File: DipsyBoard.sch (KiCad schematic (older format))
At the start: 31 parts, among them CON1 SD_Card, P1 USB_OTG, P2 CONN_01X16, P3 CONN_01X16, SW1 SW_PUSH, U1 STM32L486Rx-LQFP64, U2 LD1117S50TR, U4 PUSBMxX4, U5 TPS56x200, Y1 16MHz

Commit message: Last changes
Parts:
- removed C10, C11: 22pF, Capacitors_SMD:C_0603, symbol C_Small
- removed C15: 0.1u, Capacitors_SMD:C_0603, symbol C_Small
- removed C16: 22uF, Capacitors_SMD:C_1206, symbol C
- removed L1: 3.3uH, SMD_Packages:SMD-1210_Pol, symbol L_Small
- removed P2, P3: CONN_01X16, Pin_Headers:Pin_Header_Straight_1x16, symbol CONN_01X16
- removed R1: 33.2k, Resistors_SMD:R_0603, symbol R
- removed R2: 10.0k, Resistors_SMD:R_0603, symbol R
- removed SW1: SW_PUSH, Buttons_Switches_ThroughHole:SW_PUSH, symbol SW_PUSH
- removed U5: TPS56x200, Housings_SOT-23_SOT-143_TSOT-6:SOT-23-6, symbol TPS56x200
- removed Y1: 16MHz, Crystals:Crystal_SMD_0603_4Pads, symbol Crystal_Small
- added C18: 0.1uF, w_smd_cap:c_0603, symbol C
- added P2, P3: CONN_01X19, w_pin_strip:pin_strip_19, symbol CONN_01X19
- added P6: JTAG, engstad:conn-jtag-0.05, symbol CONN_02X05
- added SW1: RESET, Buttons_Switches_SMD:SW_SPST_EVPBF, symbol Switch_DPST
- added U3: NCP1117DT33G, w_smd_trans:sot223, symbol LD1117S50TR
- added X1: XTAL, engstad:cstce-v-c, symbol CRYSTAL_SMD
- C1, C5, C6, C7, C8, C9: footprint Capacitors_SMD:C_0603 -> w_smd_cap:c_0603
- C12, C13, C14, C2, C3, C4: footprint Capacitors_SMD:C_0805 -> w_smd_cap:c_0805
- C17: footprint Capacitors_SMD:C_1206 -> w_smd_cap:c_1206
- CON1: footprint Connect:SD_Card_Receptacle -> xess:xess-SCHD3A0100
- P1: footprint Connect:USB_B -> w_conn_pc:conn_usb_B_mini_smd
- U2: value LD1117S50TR -> NCP1117ST50T3G; footprint Housings_SOT-23_SOT-143_TSOT-6:SOT-23 -> w_smd_trans:sot223
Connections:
- net labels added: +5V, OTG_FS_D+, OTG_FS_D-, PVD
- net labels removed: D4/PVD, OTG_FS_DM, OTG_FS_DP, OTG_FS_SOF, OTG_FS_VBUS, SENSE, SW
- wire segments 65 -> 57
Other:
- moved on the sheet: C14, C17

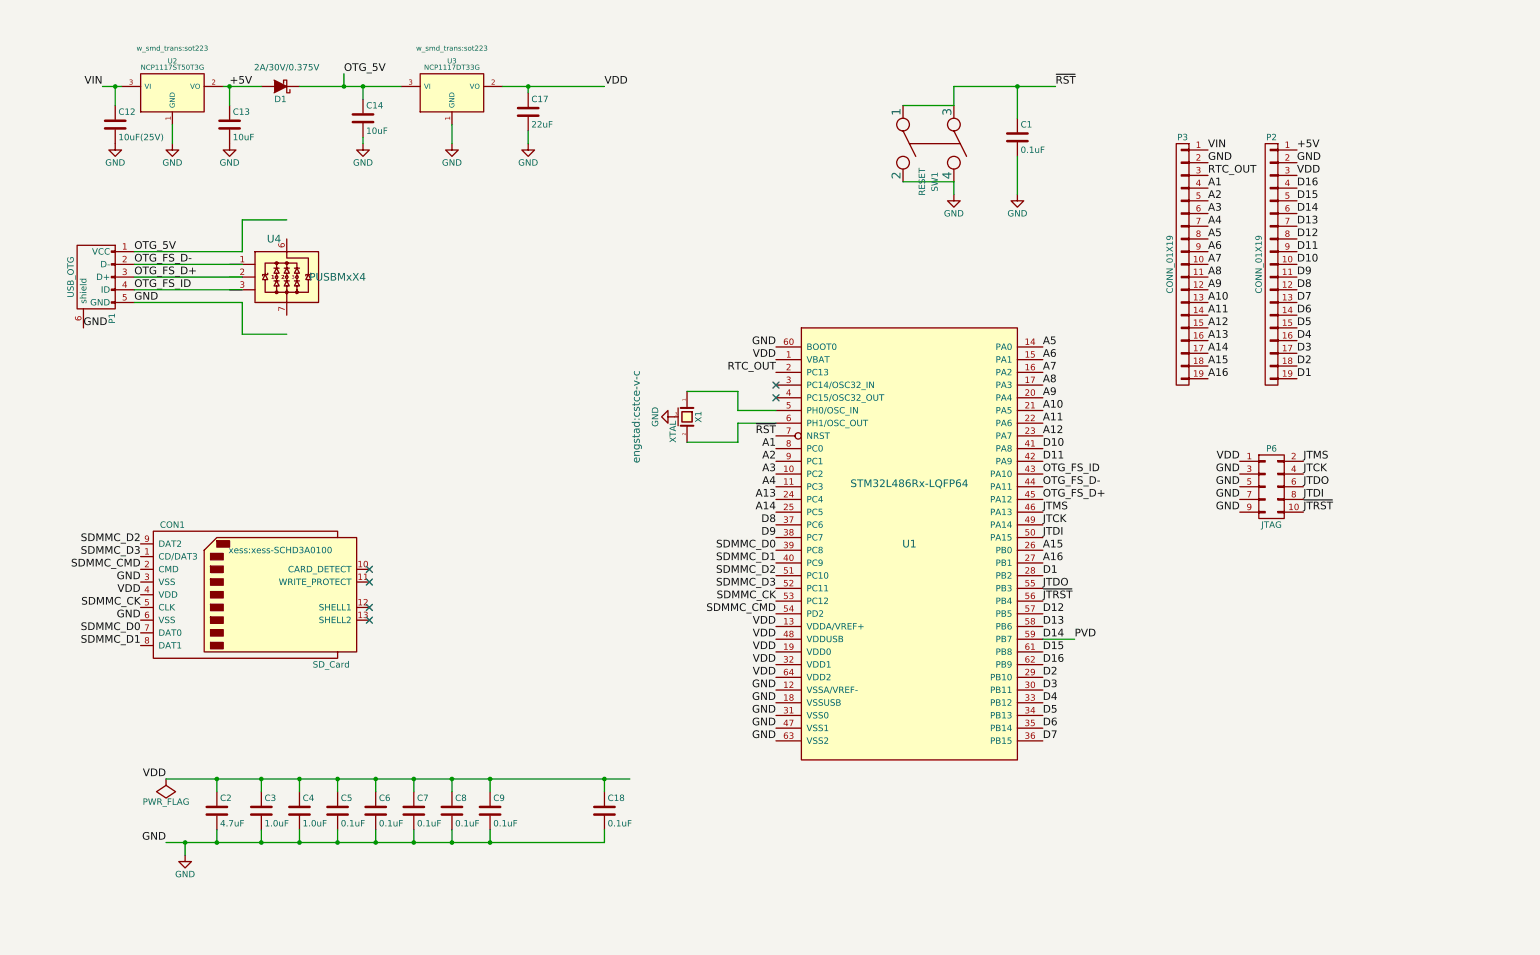
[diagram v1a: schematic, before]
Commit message: Changes of power source
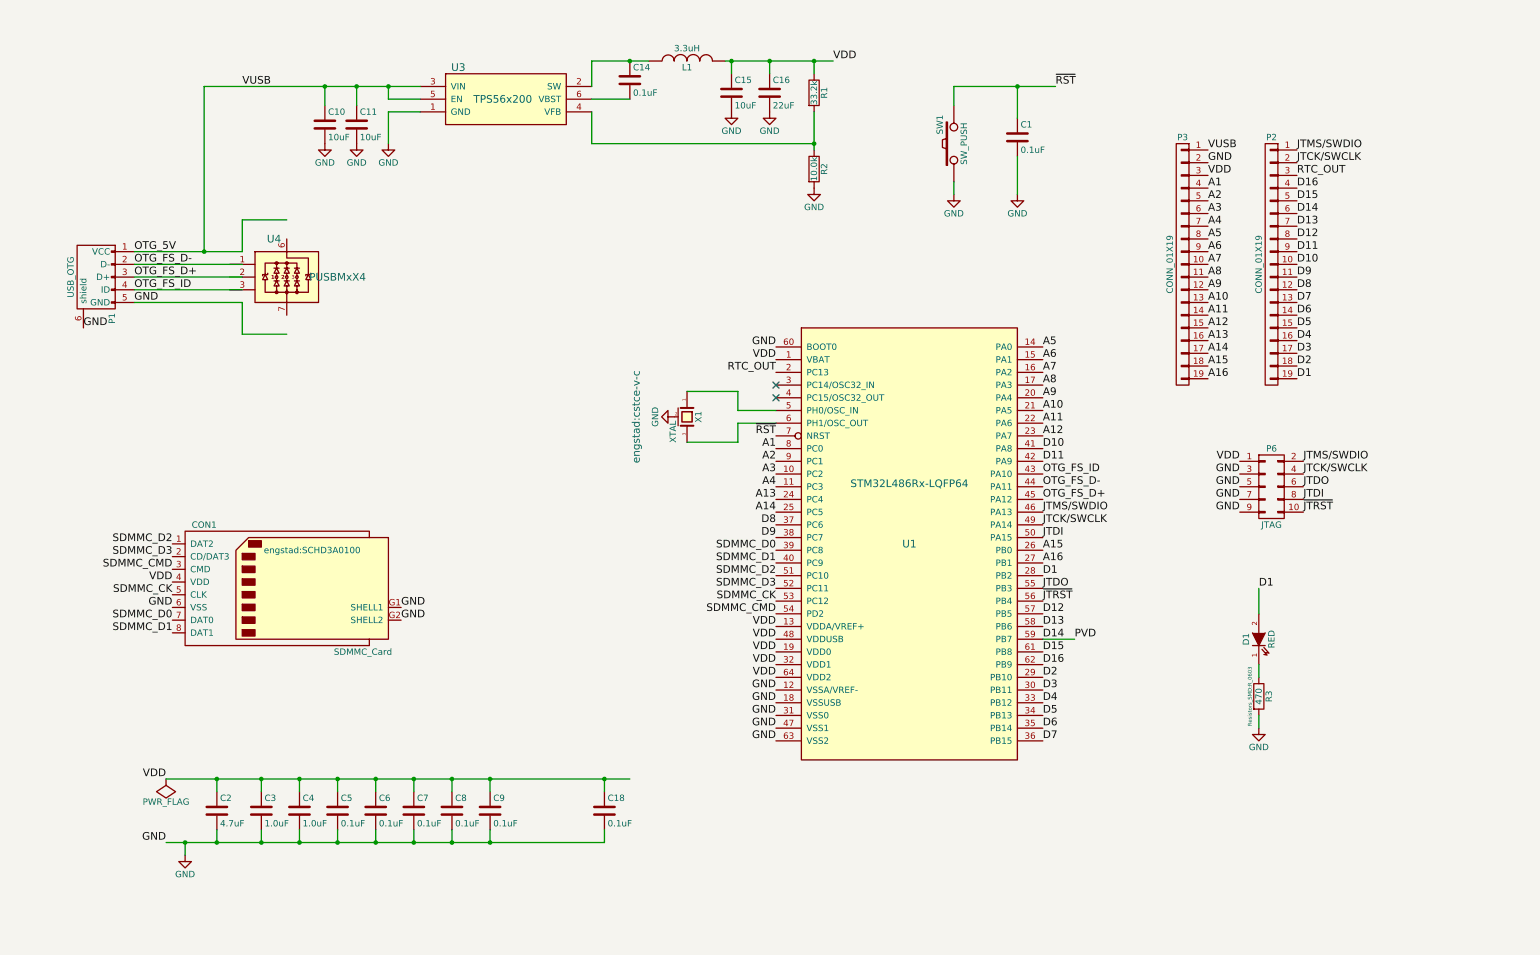
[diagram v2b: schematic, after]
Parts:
- removed C12: 10uF(25V), w_smd_cap:c_0805, symbol C
- removed C13: 10uF, w_smd_cap:c_0805, symbol C
- removed C17: 22uF, w_smd_cap:c_1206, symbol C
- removed CON1: SD_Card, xess:xess-SCHD3A0100, symbol SD_Card
- removed D1: 2A/30V/0.375V, Diodes_SMD:SOD-123, symbol D_Schottky
- removed SW1: RESET, Buttons_Switches_SMD:SW_SPST_EVPBF, symbol Switch_DPST
- removed U2: NCP1117ST50T3G, w_smd_trans:sot223, symbol LD1117S50TR
- removed U3: NCP1117DT33G, w_smd_trans:sot223, symbol LD1117S50TR
- removed X1: XTAL, engstad:cstce-v-c, symbol CRYSTAL_SMD
- added C10, C11, C15: 10uF, Capacitors_SMD:C_0805, symbol C
- added C16: 22uF, Capacitors_SMD:C_1206, symbol C
- added CON1: SDMMC_Card, engstad:SCHD3A0100, symbol SDMMC_Card
- added D1: RED, LEDs:LED-0805, symbol LED
- added L1: 3.3uH, engstad:inductor-smd-1212, symbol INDUCTOR
- added R1: 33.2k, Resistors_SMD:R_0603, symbol R
- added R2: 10.0k, Resistors_SMD:R_0603, symbol R
- added R3: 470, Resistors_SMD:R_0603, symbol R
- added SW1: SW_PUSH, engstad:tactile-switch-te-147873-2, symbol SW_PUSH
- added U3: TPS56x200, Housings_SOT-23_SOT-143_TSOT-6:SOT-23-6, symbol TPS56x200
- added X1: XTAL, engstad:cstce-v-c, symbol crystal-resonator-smd
- C1, C18, C5, C6, C7, C8, C9: footprint w_smd_cap:c_0603 -> Capacitors_SMD:C_0603
- C14: value 10uF -> 0.1uF; footprint w_smd_cap:c_0805 -> Capacitors_SMD:C_0603
- C2, C3, C4: footprint w_smd_cap:c_0805 -> Capacitors_SMD:C_0805
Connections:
- net labels added: JTCK/SWCLK, JTMS/SWDIO, VUSB
- net labels removed: +5V, JTCK, JTMS, VIN
- wire segments 57 -> 63
- no-connect marks 6 -> 2

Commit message: latest - including v0.1
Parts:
- added C? (x2): 22uF, Capacitors_SMD:C_0805, symbol C
- added L?: 470nF, symbol L_Small
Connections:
- wire segments 63 -> 75
- no-connect marks 2 -> 3
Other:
- moved on the sheet: CON1
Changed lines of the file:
@@
 Text Label 6450 4800 2    60   ~ 0
 SDMMC_D1
-Text Label 1700 5250 2    60   ~ 0
+Text Label 4650 5250 0    60   ~ 0
 SDMMC_D0
-Text Label 1700 5350 2    60   ~ 0
+Text Label 4650 5350 0    60   ~ 0
 SDMMC_D1
-Text Label 1700 4650 2    60   ~ 0
+Text Label 4650 4650 0    60   ~ 0
 SDMMC_D2
-Text Label 1700 4750 2    60   ~ 0
+Text Label 4650 4750 0    60   ~ 0
 SDMMC_D3
-Text Label 1700 4850 2    60   ~ 0
+Text Label 4650 4850 0    60   ~ 0
 SDMMC_CMD
-Text Label 1700 5050 2    60   ~ 0
+Text Label 4650 5050 0    60   ~ 0
 SDMMC_CK
 Text Label 6450 5200 2    60   ~ 0
@@
 Text Label 6450 4900 2    60   ~ 0
 SDMMC_D2
-Text Label 3500 5150 0    60   ~ 0
+Text Label 900  5150 2    60   ~ 0
 GND
-Text Label 1700 4950 2    60   ~ 0
+Text Label 4650 4950 0    60   ~ 0
 VDD
-Text Label 1700 5150 2    60   ~ 0
+Text Label 2700 5150 0    60   ~ 0
 GND
 Text Label 8550 3100 0    60   ~ 0
@@
 	2600 2100 2250 2100
 Wire Wire Line
-	2250 2100 2250 2350
-Wire Wire Line
-	2250 2350 1400 2350
+	2250 2350 2250 2100
+Wire Wire Line
+	1400 2350 2250 2350
 Text Label 1400 2350 0    60   ~ 0
 OTG_5V
@@
 Text Label 10100 4400 2    60   ~ 0
 GND
-Text Label 10100 4300 2    60   ~ 0
-GND
 Text Label 9850 1750 0    60   ~ 0
 VDD
 Text Label 9850 1650 0    60   ~ 0
 GND
-Text Label 10550 1750 0    60   ~ 0
-RTC_OUT
 $Comp
 L CONN_01X19 P2
@@
 	0    -1   -1   0
 $EndComp
-Text Label 3500 5250 0    60   ~ 0
+Text Label 900  5250 2    60   ~ 0
 GND
 $Comp
 L SDMMC_Card CON1
 U 1 1 560A8328
-P 2600 5050
-F 0 "CON1" H 1950 5600 50  0000 C CNN
-F 1 "SDMMC_Card" H 3200 4600 50  0000 C CNN
-F 2 "engstad:SCHD3A0100" H 2800 5400 50  0000 C CNN
-F 3 "" H 2600 5050 60  0000 C CNN
-	1    2600 5050
-	1    0    0    -1
+P 1800 5050
+F 0 "CON1" H 1150 5600 50  0000 C CNN
+F 1 "SDMMC_Card" H 2400 4600 50  0000 C CNN
+F 2 "engstad:SCHD3A0100" H 2000 5400 50  0000 C CNN
+F 3 "" H 1800 5050 60  0000 C CNN
+	1    1800 5050
+	-1   0    0    -1
 $EndComp
 $Comp
@@
 $EndComp
 Wire Wire Line
-	6750 1550 6750 1250
+	6750 1250 6750 1550
 Wire Wire Line
 	5000 1250 5000 1500
@@
 Text Label 10250 5000 0    60   ~ 0
 D1
+Wire Wire Line
+	2700 4950 4400 4950
+$Comp
+L C C?
+U 1 1 56166412
+P 4000 5600
+F 0 "C?" H 4025 5700 50  0000 L CNN
+F 1 "22uF" H 4025 5500 50  0000 L CNN
+F 2 "Capacitors_SMD:C_0805" H 4038 5450 30  0001 C CNN
+F 3 "" H 4000 5600 60  0000 C CNN
+	1    4000 5600
+	1    0    0    -1
+$EndComp
+$Comp
+L C C?
+U 1 1 56166609
+P 4250 5600
+F 0 "C?" H 4275 5700 50  0000 L CNN
+F 1 "22uF" H 4275 5500 50  0000 L CNN
+F 2 "Capacitors_SMD:C_0805" H 4288 5450 30  0001 C CNN
+F 3 "" H 4250 5600 60  0000 C CNN
+	1    4250 5600
+	1    0    0    -1
+$EndComp
+Wire Wire Line
+	4000 5450 4000 4950
+Connection ~ 4000 4950
+Wire Wire Line
+	4000 5750 4000 5800
+Wire Wire Line
+	4250 5750 4250 5800
+Wire Wire Line
+	4250 5450 4250 4950
+Connection ~ 4250 4950
+$Comp
+L GND #PWR?
+U 1 1 5616688A
+P 4000 5800
+F 0 "#PWR?" H 4000 5550 50  0001 C CNN
+F 1 "GND" H 4000 5650 50  0000 C CNN
+F 2 "" H 4000 5800 60  0000 C CNN
+F 3 "" H 4000 5800 60  0000 C CNN
+	1    4000 5800
+	1    0    0    -1
+$EndComp
+$Comp
+L GND #PWR?
+U 1 1 561668FC
+P 4250 5800
+F 0 "#PWR?" H 4250 5550 50  0001 C CNN
+F 1 "GND" H 4250 5650 50  0000 C CNN
+F 2 "" H 4250 5800 60  0000 C CNN
+F 3 "" H 4250 5800 60  0000 C CNN
+	1    4250 5800
+	1    0    0    -1
+$EndComp
+$Comp
+L L_Small L?
+U 1 1 561669CE
+P 4500 4950
+F 0 "L?" H 4530 4990 50  0000 L CNN
+F 1 "470nF" H 4530 4910 50  0000 L CNN
+F 2 "" H 4500 4950 60  0000 C CNN
+F 3 "" H 4500 4950 60  0000 C CNN
+	1    4500 4950
+	0    -1   -1   0
+$EndComp
+Wire Wire Line
+	4600 4950 4650 4950
+Wire Wire Line
+	2700 4650 4650 4650
+Wire Wire Line
+	2700 4750 4650 4750
+Wire Wire Line
+	2700 4850 4650 4850
+Wire Wire Line
+	2700 5050 4650 5050
+Wire Wire Line
+	2700 5250 4650 5250
+Wire Wire Line
+	2700 5350 4650 5350
+Text Label 10550 1750 0    60   ~ 0
+~JTRST
+NoConn ~ 10100 4300
 $EndSCHEMATC

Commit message: v0.2
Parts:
- removed C14: 0.1uF, Capacitors_SMD:C_0603, symbol C
- removed C15: 10uF, Capacitors_SMD:C_0805, symbol C
- removed C16: 22uF, Capacitors_SMD:C_1206, symbol C
- removed L1: 3.3uH, engstad:inductor-smd-1212, symbol INDUCTOR
- removed P2, P3: CONN_01X19, w_pin_strip:pin_strip_19, symbol CONN_01X19
- removed R1: 33.2k, Resistors_SMD:R_0603, symbol R
- removed R2: 10.0k, Resistors_SMD:R_0603, symbol R
- removed U3: TPS56x200, Housings_SOT-23_SOT-143_TSOT-6:SOT-23-6, symbol TPS56x200
- added C17, C19: 10pF, smd:SM0603, symbol C_Small
- added D2: DFLS240L, engstad:diode-smd-powerdi-123, symbol D_Schottky_Small
- added D3: GREEN, LEDs:LED-0805, symbol LED
- added JP1: JUMPER3, xess:xess-JP2, symbol JUMPER3
- added L3: Bead, smd:SM0805, symbol L_Small
- added P2: Analog, Pin_Headers:Pin_Header_Straight_1x16, symbol CONN_01X16
- added P3: Digital, Pin_Headers:Pin_Header_Straight_1x16, symbol CONN_01X16
- added P4: JLINK-SWD, xess:HDR_1x6, symbol CONN_01X06
- added P5: POWER, w_pin_strip:pin_socket_2, symbol CONN_01X02
- added R4: 10k, smd:SM0603, symbol R
- added R5: 470, smd:SM0603, symbol R
- added U2: NCP1117ST33T3G, TO_SOT_Packages_SMD:SOT-223, symbol NCP1117ST33T3G
- added U3: APX823, TO_SOT_Packages_SMD:SOT-23-5, symbol APX823
- added Y1: Crystal, armory:CRYSTAL-32k-B, symbol Crystal
- C1, C18, C5, C6, C7, C8, C9: footprint Capacitors_SMD:C_0603 -> smd:SM0603
- C10, C11, C2: footprint Capacitors_SMD:C_0805 -> smd:SM0805
- C12, C13: renamed from C?; footprint Capacitors_SMD:C_0805 -> smd:SM1206
- C3, C4: footprint Capacitors_SMD:C_0805 -> smd:SM0603
- L2: renamed from L?; value 470nF -> 470nH; footprint (none) -> smd:SM0603
- P1: footprint w_conn_pc:conn_usb_B_mini_smd -> engstad:usb-otg-short
- P6: value JTAG -> CORTEX-JTAG; footprint engstad:conn-jtag-0.05 -> engstad:smt-pin-header-02x05-127
- R3: footprint Resistors_SMD:R_0603 -> smd:SM0603
- U4: value PUSBMxX4 -> PUSBM5V5X4; footprint Housings_DFN_QFN:DFN-6-1EP_2x2mm_Pitch0.5mm -> engstad:dfn1616-6
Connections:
- net labels added: +3.3VADC, BOOT0, JTDO/SWO, RTC, RTC_OSC_IN, RTC_OSC_OUT, VDDA
- net labels removed: JTDO, RTC_OUT, ~JTRST
- wire segments 75 -> 96
- no-connect marks 3 -> 2
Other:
- note added: "JTCK/SWCLK: (PA14) Morpho Pin 15 (Row 8L)\nJTMS/SWDIO: (PA13) Morpho Pin 13 (Row 3L)\n~RST~: Arduino pin\n\n"
- moved on the sheet: C1, C10, C11, C12, C13, C4, C9, CON1, D1, L2, P1, P6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

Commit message: More work
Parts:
- removed D2: DFLS240L, engstad:diode-smd-powerdi-123, symbol D_Schottky_Small
- removed U2: NCP1117ST33T3G, TO_SOT_Packages_SMD:SOT-223, symbol NCP1117ST33T3G
- added C14: 1nF, smd:SM0603, symbol C
- added C16: 10uF, smd:SM0805, symbol C
- added L1: 1.5uH, engstad:inductor-smd-1212, symbol INDUCTOR_SMALL
- added R1: 560k, smd:SM0603, symbol R_Small
- added R2: 180k, smd:SM0603, symbol R_Small
- added R6: 1M, smd:SM0603, symbol R
- added U2: TPS63051, engstad:dsbga-12, symbol TPS63051
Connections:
- net GND: now also C14.2, C16.2, R2.2, U2.B1 (GND), U2.B2 (ILIM0), U2.C2 (PFM/PWM)
- net OTG_5V: now also U2.A2 (VIN), U2.A3 (EN), U2.B3 (ILIM1)
- net VDD: now also C16.1, R1.1, R6.1, U2.D1 (VOUT)
- new net: L1.1, U2.A1 (L1)
- new net: L1.2, U2.C1 (L2)
- new net: R1.2, R2.1, U2.D2 (FB)
- new net: C14.1, U2.D3 (SS)
- new net PG: R6.2, U2.C3 (PG)
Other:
- moved on the sheet: C1, C10, C11, C12, C13, C17, C18, C19, C2, C3, C4, C5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
